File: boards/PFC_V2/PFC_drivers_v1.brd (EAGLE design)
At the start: 82.6 x 50.8 mm, 35 parts

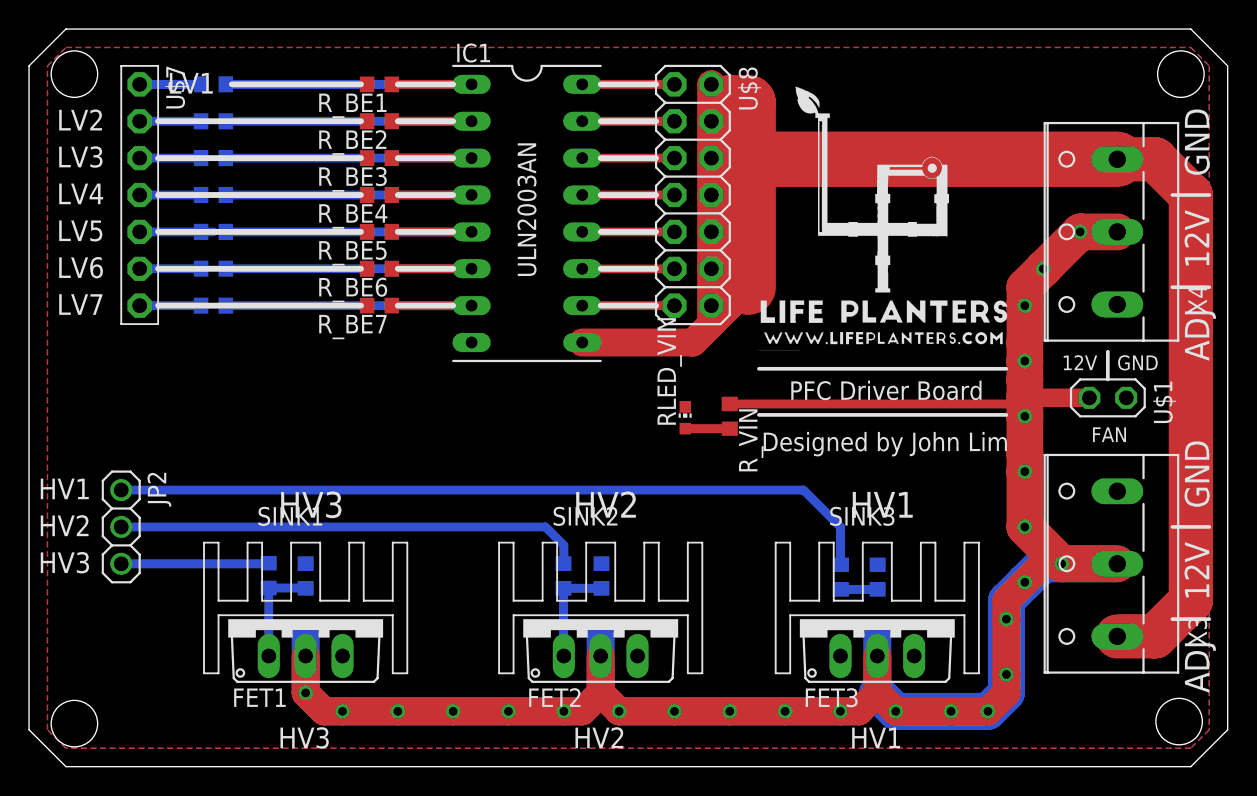
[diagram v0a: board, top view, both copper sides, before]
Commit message: fixed problem with the power fet driver
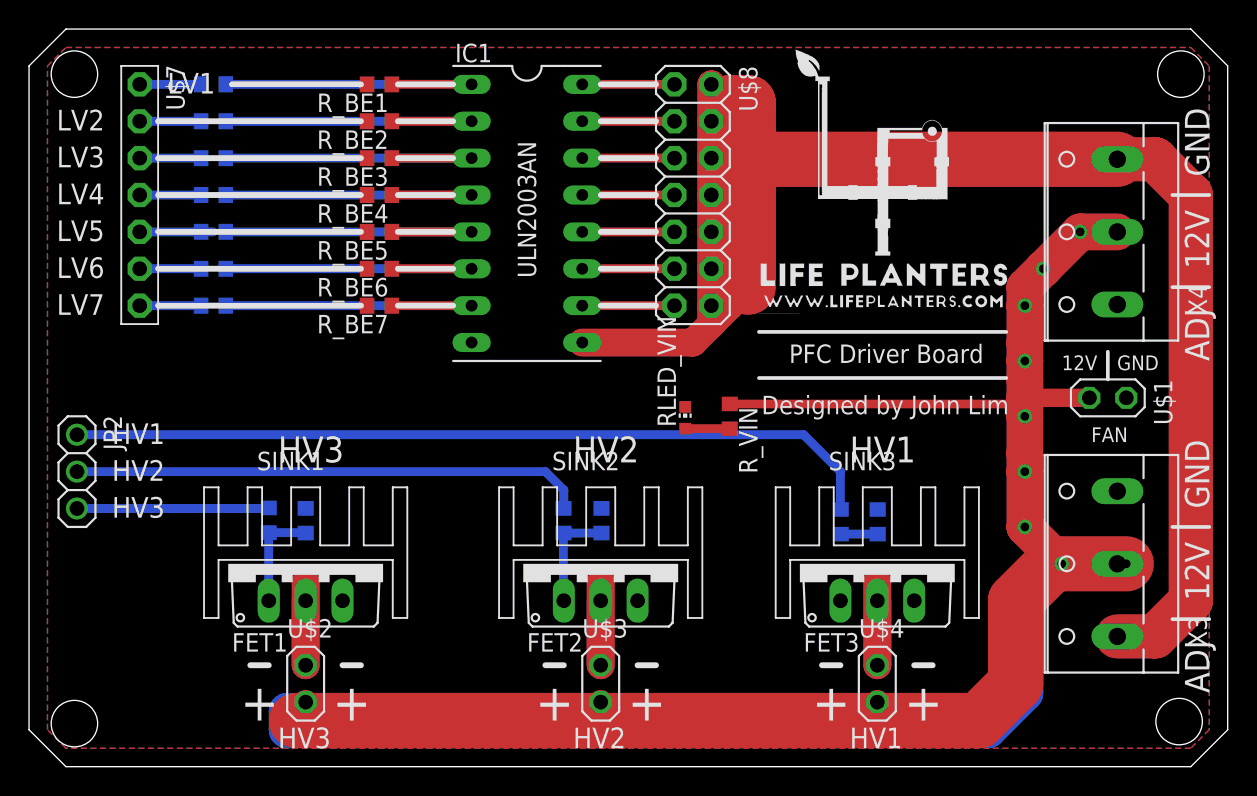
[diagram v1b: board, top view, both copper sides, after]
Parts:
- added U$2, U$3, U$4: PINHD-2X1, pinhead:2X01
- moved JP2 4.88 mm to (18.5, 47.0)
- moved FET1 3.81 mm to (34.3, 40.6)
- moved FET2 3.81 mm to (54.6, 40.6)
- moved FET3 3.81 mm to (73.7, 40.6)
- moved R_GS1 3.81 mm to (34.3, 43.6)
- moved R_GS2 3.81 mm to (54.7, 43.6)
- moved R_GS3 3.81 mm to (73.7, 43.5)
- moved R_IN1 3.81 mm to (31.8, 43.6)
- moved R_IN2 3.81 mm to (52.0, 43.6)
- moved R_IN3 3.81 mm to (71.1, 43.5)
- moved SINK1 3.81 mm to (34.3, 41.9)
- moved SINK2 3.81 mm to (54.6, 41.9)
- moved SINK3 3.81 mm to (73.7, 41.9)
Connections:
- new net N$15: FET1.C, U$2.2
- new net N$16: FET2.C, U$3.2
- new net N$17: FET3.C, U$4.2
- net VIN: now also U$2.1, U$3.1, U$4.1; no longer FET1.C, FET2.C, FET3.C
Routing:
- net VIN: track 206.3 -> 283.6 mm, vias 25 -> 9
- net N$17: track 0.00 -> 10.2 mm
- net N$16: track 0.00 -> 10.2 mm
- net N$15: track 0.00 -> 10.2 mm
- net G3: track 53.2 -> 56.2 mm
- net G2: track 32.3 -> 35.3 mm
- net G1: track 10.2 -> 13.2 mm
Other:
- board text added: "+"

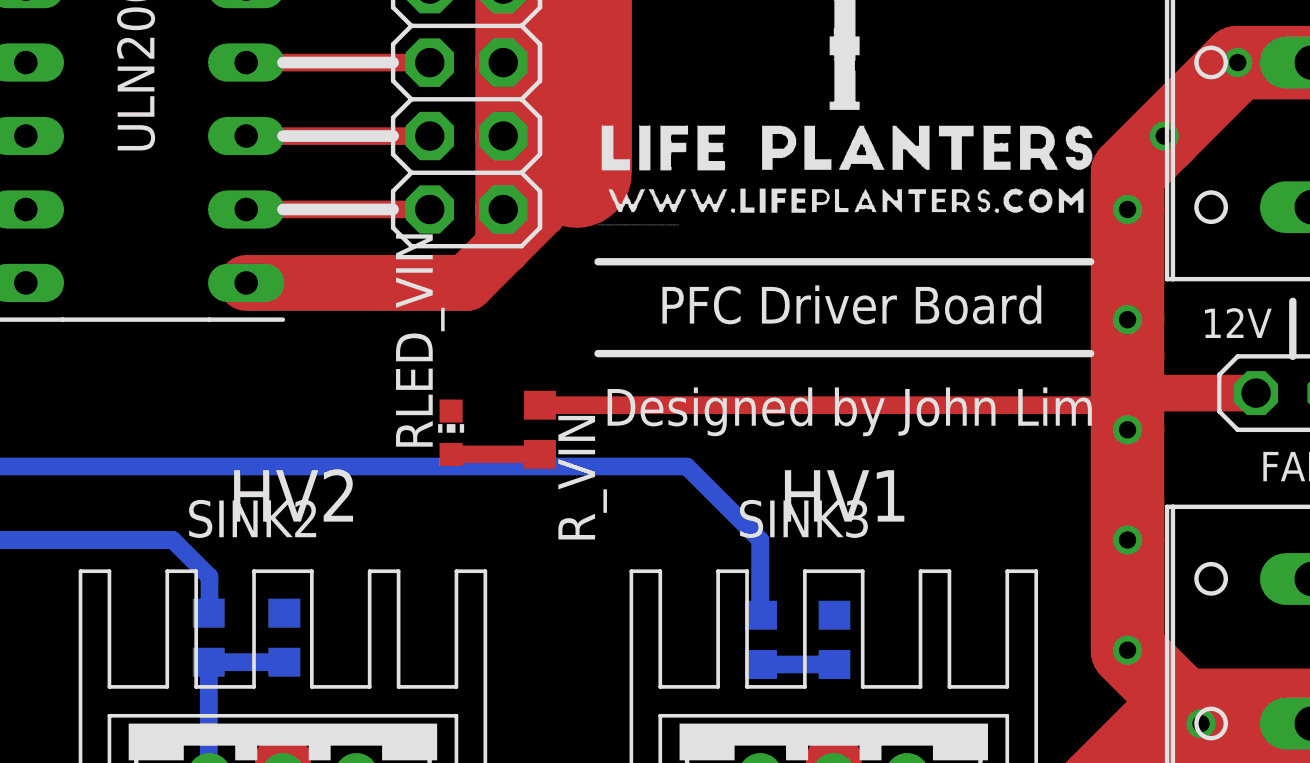
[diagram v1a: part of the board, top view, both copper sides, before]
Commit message: completed ui of touch screen. No integration yet
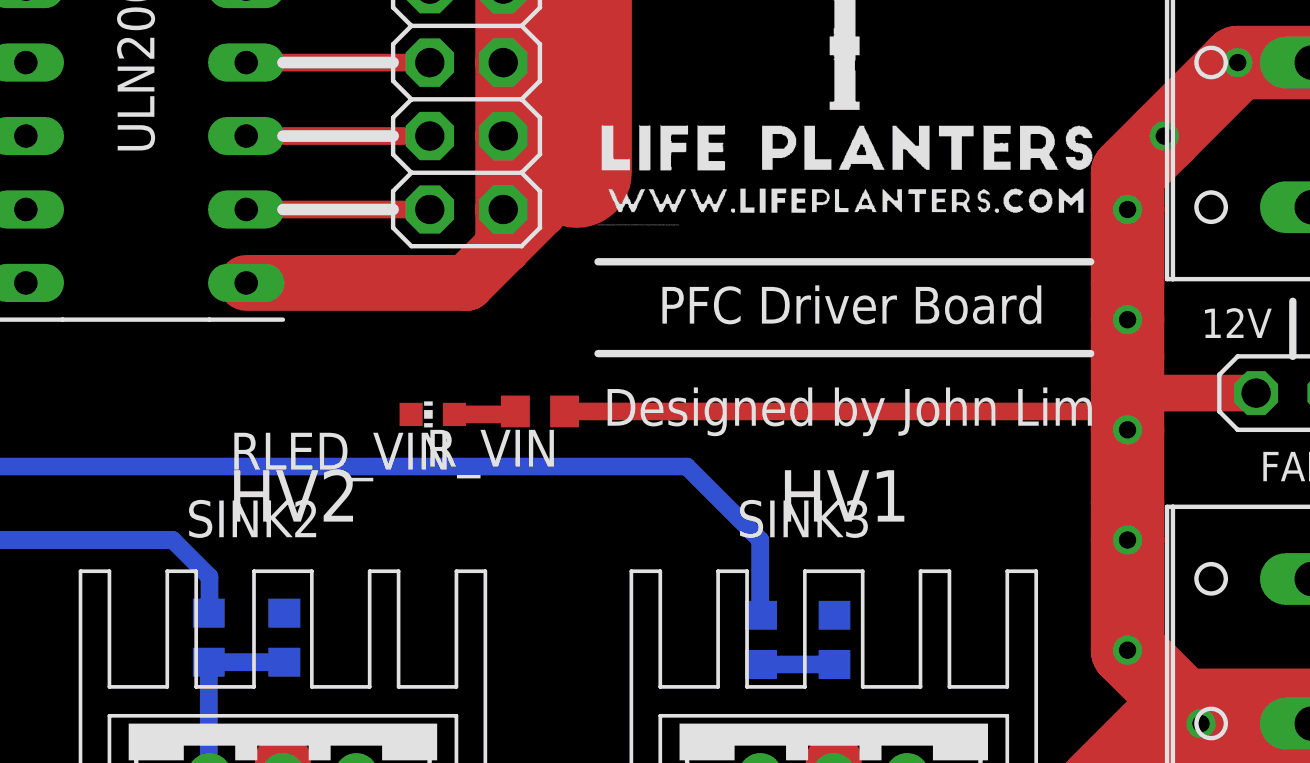
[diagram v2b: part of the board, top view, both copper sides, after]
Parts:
- moved RLED_VIN 0.90 mm to (59.8, 51.3), turned to 90 degrees
- moved R_VIN 0.64 mm to (63.5, 51.4), turned to 180 degrees
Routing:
- net N$1: track 3.07 -> 2.15 mm
- net VIN: track 283.6 -> 282.8 mm
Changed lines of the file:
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@@
 <element name="IC1" library="ic-package" package="SOCKET-16" value="" x="49.53" y="64.77" rot="R270"/>
 <element name="JP2" library="adafruit" package="1X03" value="" x="18.542" y="46.99" rot="R270"/>
-<element name="RLED_VIN" library="led" package="CHIP-LED0603" value="" x="60.4266" y="50.6984"/>
+<element name="RLED_VIN" library="led" package="CHIP-LED0603" value="" x="59.7916" y="51.3334" rot="R90"/>
 <element name="R_BE1" library="resistor" package="R0603" value="10k" x="39.37" y="73.66" rot="R180"/>
 <element name="R_BE2" library="resistor" package="R0603" value="10k" x="39.37" y="71.12" rot="R180"/>
@@
 <element name="R_IN2" library="resistor" package="R0603" value="50" x="52.0446" y="43.6118" rot="MR270"/>
 <element name="R_IN3" library="resistor" package="R0603" value="50" x="71.1454" y="43.5356" rot="MR270"/>
-<element name="R_VIN" library="resistor" package="R0603" value="1k" x="63.5" y="50.8" rot="R270"/>
+<element name="R_VIN" library="resistor" package="R0603" value="1k" x="63.5" y="51.435" rot="R180"/>
 <element name="SINK1" library="heatsink" package="FW1S" value="FW1S" x="34.29" y="41.91"/>
 <element name="SINK2" library="heatsink" package="FW1S" value="FW1S" x="54.61" y="41.91"/>
@@
 <contactref element="R_BE6" pad="2"/>
 <contactref element="R_BE7" pad="2"/>
-<polygon width="0.4064" layer="16">
+<polygon width="0.4064" layer="16" isolate="0.4064">
 <vertex x="16.51" y="29.21"/>
 <vertex x="16.51" y="74.93"/>
@@
 <vertex x="17.78" y="27.94"/>
 </polygon>
-<polygon width="0.4064" layer="1">
+<polygon width="0.4064" layer="1" isolate="0.4064">
 <vertex x="16.51" y="74.93"/>
 <vertex x="17.78" y="76.2"/>
@@
 <via x="83.82" y="58.42" extent="1-16" drill="0.6" shape="octagon"/>
 <via x="85.09" y="60.96" extent="1-16" drill="0.6" shape="octagon"/>
-<wire x1="63.5" y1="51.65" x2="83.4" y2="51.65" width="0.6096" layer="1"/>
-<wire x1="83.4" y1="51.65" x2="83.82" y2="52.07" width="0.6096" layer="1"/>
+<wire x1="83.185" y1="51.435" x2="83.82" y2="52.07" width="0.6096" layer="1"/>
 <contactref element="U$1" pad="1"/>
 <wire x1="88.265" y1="52.07" x2="83.82" y2="52.07" width="1.27" layer="1"/>
@@
 <wire x1="54.61" y1="30.48" x2="73.66" y2="30.48" width="1.6764" layer="1"/>
 <wire x1="73.66" y1="31.115" x2="73.66" y2="30.48" width="1.6764" layer="1"/>
-<wire x1="90.17" y1="40.64" x2="90.19" y2="40.64" width="0" layer="19" extent="1-1"/>
 <wire x1="80.645" y1="29.845" x2="74.295" y2="29.845" width="1.6764" layer="1"/>
 <wire x1="74.295" y1="29.845" x2="73.66" y2="30.48" width="1.6764" layer="1"/>
 <wire x1="33.655" y1="29.845" x2="34.29" y2="29.21" width="1.6764" layer="1"/>
+<wire x1="64.35" y1="51.435" x2="83.185" y2="51.435" width="0.6096" layer="1"/>
+<wire x1="90.17" y1="40.64" x2="90.19" y2="40.64" width="0" layer="19" extent="1-1"/>
 </signal>
 <signal name="N$1">
 <contactref element="RLED_VIN" pad="A"/>
 <contactref element="R_VIN" pad="2"/>
-<wire x1="60.4266" y1="49.9484" x2="63.4984" y2="49.9484" width="0.6096" layer="1"/>
-<wire x1="63.4984" y1="49.9484" x2="63.5" y2="49.95" width="0.6096" layer="1"/>
+<wire x1="60.5416" y1="51.3334" x2="62.5484" y2="51.3334" width="0.6096" layer="1"/>
+<wire x1="62.5484" y1="51.3334" x2="62.65" y2="51.435" width="0.6096" layer="1"/>
 </signal>
 <signal name="V_ADJ">
